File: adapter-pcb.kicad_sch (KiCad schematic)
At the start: 7 parts, among them J3 SS5-80-3.50-X-D-K-XX, M1 MountingHole_Pad_MP, M2 MountingHole_Pad_MP, M3 MountingHole_Pad_MP, M4 MountingHole_Pad_MP

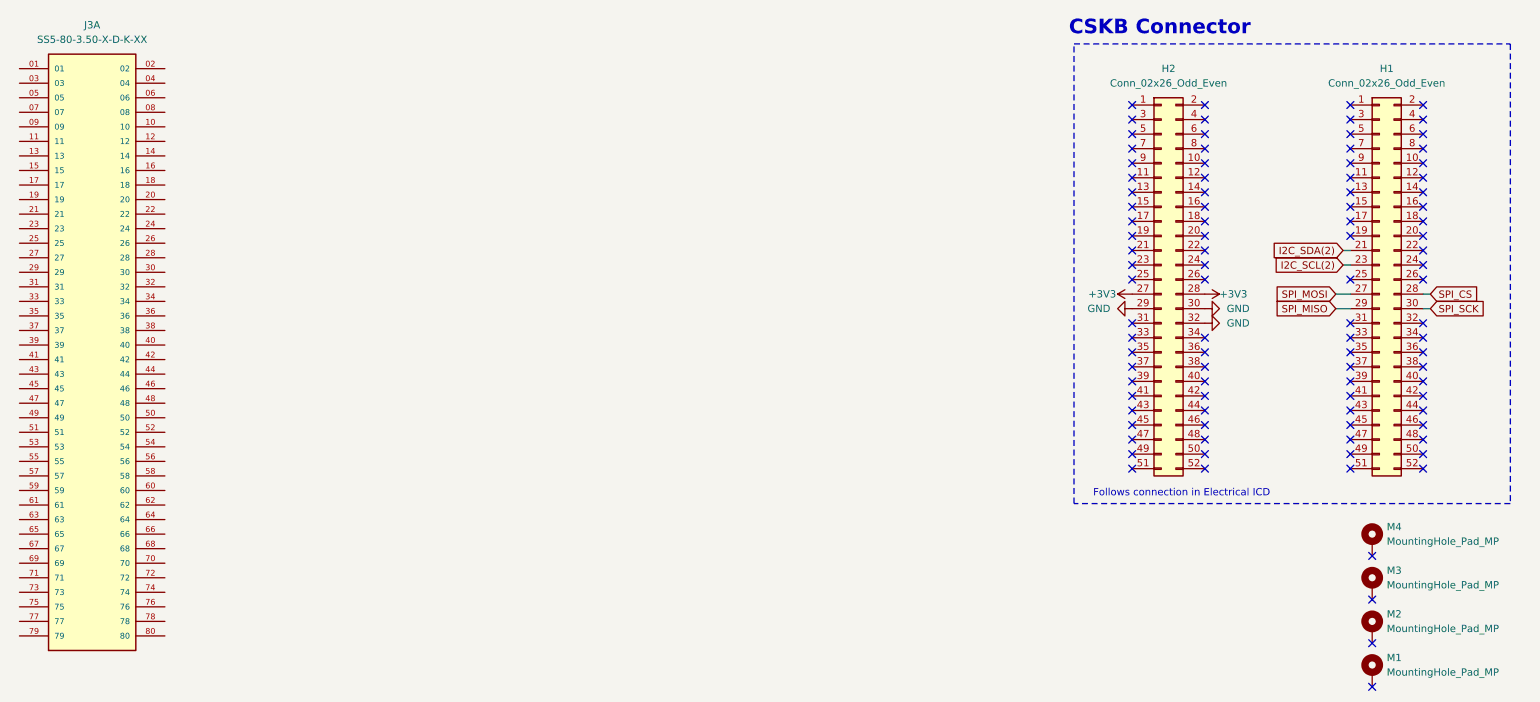
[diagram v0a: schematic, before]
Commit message: Routed PCB (with I2C buffer)
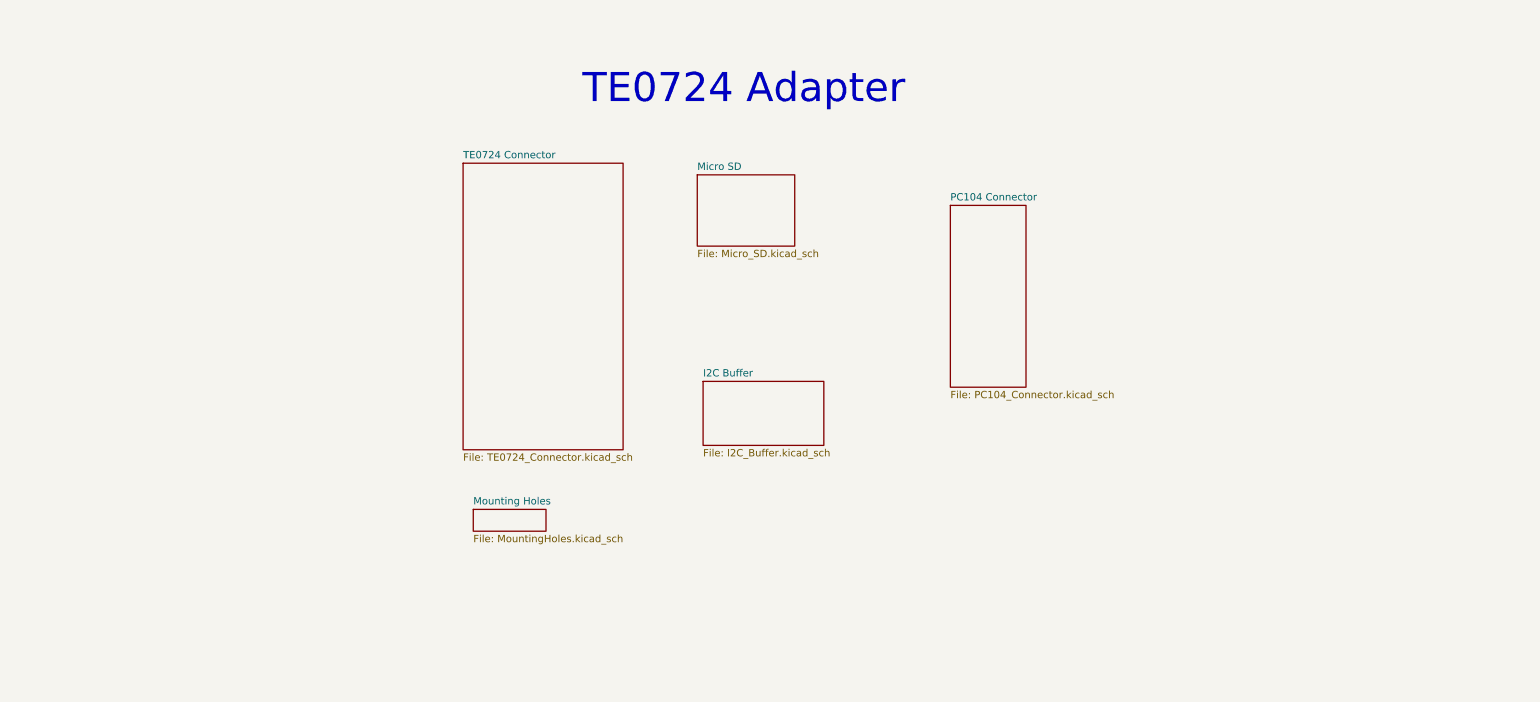
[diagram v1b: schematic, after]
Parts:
- removed H1, H2: Conn_02x26_Odd_Even, adapter:RHDR52W64P254_2X26_6654X495X1135P, symbol Connector_Generic:Conn_02x26_Odd_Even
- removed J3: SS5-80-3.50-X-D-K-XX, adapter:SAMTEC_SS5-80-3.50-X-D-K-XX, symbol adapter:SS5-80-3.50-X-D-K-XX
- removed M1, M2, M3, M4: MountingHole_Pad_MP, adapter:MountingHole_3.18mm_6.35mm_Pad, symbol Mechanical:MountingHole_Pad_MP
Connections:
- no-connect marks 97 -> 0
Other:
- added sheet I2C Buffer (I2C_Buffer.kicad_sch)
- added sheet Micro SD (Micro_SD.kicad_sch)
- added sheet Mounting Holes (MountingHoles.kicad_sch)
- added sheet PC104 Connector (PC104_Connector.kicad_sch)
- added sheet TE0724 Connector (TE0724_Connector.kicad_sch)
- note added: "TE0724 Adapter"
- note removed: "CSKB Connector"
- note removed: "Follows connection in Electrical ICD"
- title: (none) -> Overview

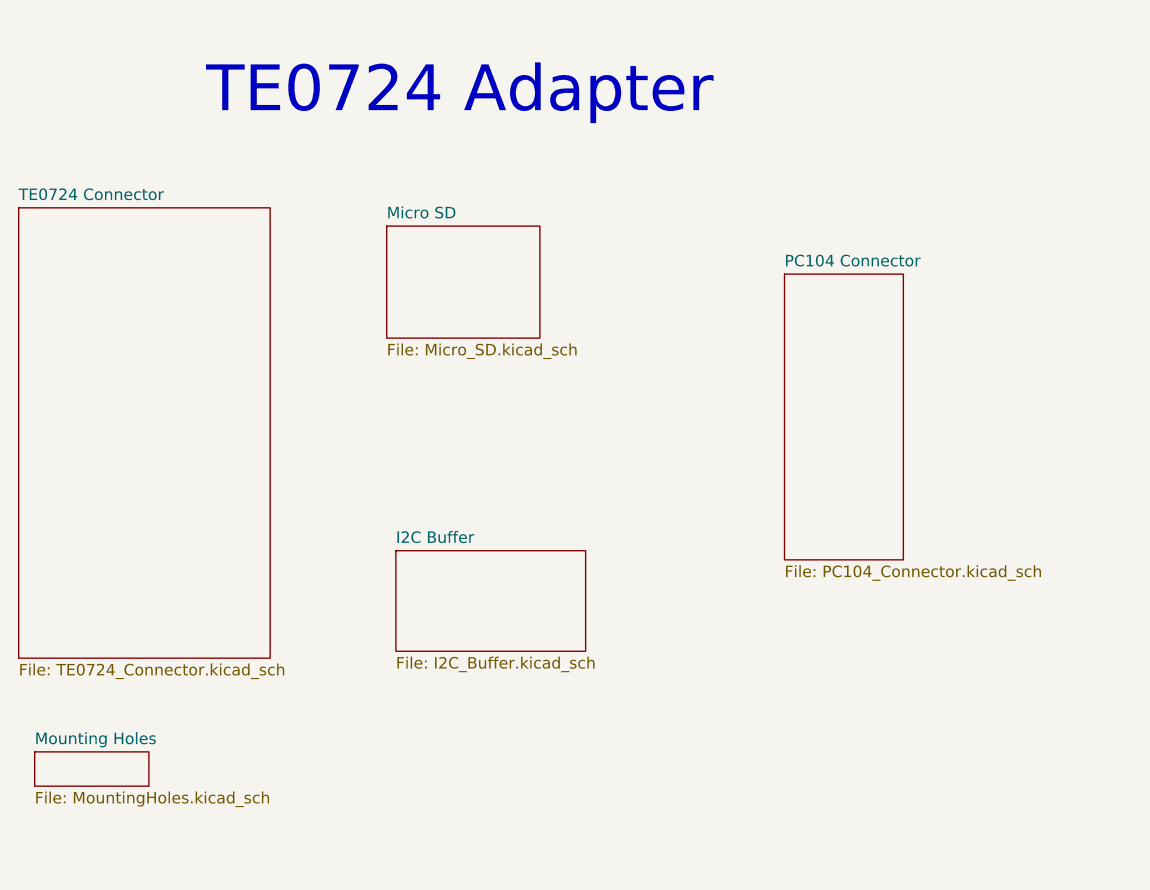
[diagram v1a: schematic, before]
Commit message: Fixed GND issues with connector and mounting holes
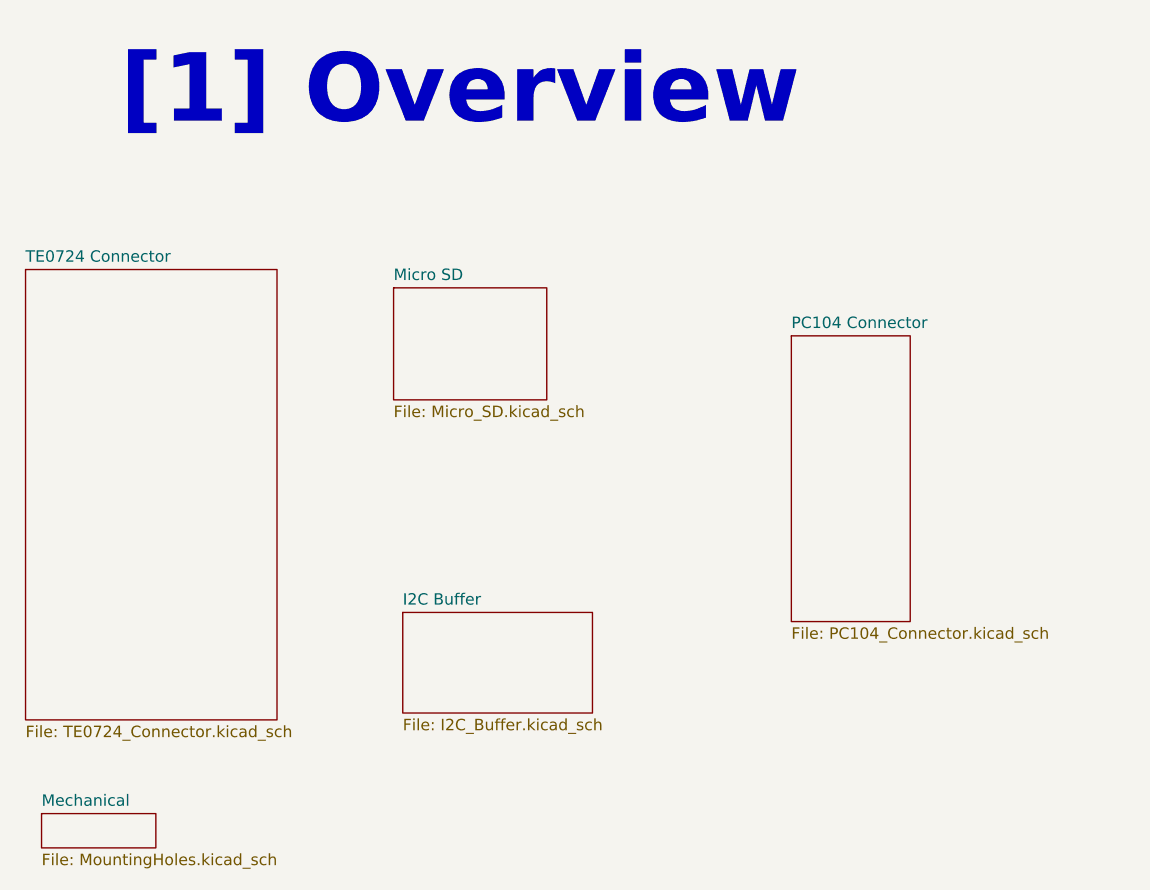
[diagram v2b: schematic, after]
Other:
- sheet Mounting Holes renamed Mechanical
- note added: "[1] Overview"
- note removed: "TE0724 Adapter"
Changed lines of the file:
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@@
 		(title "Overview")
 	)
-	(text "TE0724 Adapter"
+	(text "[1] Overview"
 		(exclude_from_sim no)
 		(at 146.812 27.686 0)
 		(effects
 			(font
-				(size 5.08 5.08)
-				(thickness 0.635)
-			)
-		)
-	)
-	(sheet
-		(at 138.684 42.672)
+				(size 7.62 7.62)
+				(thickness 1.524)
+				(bold yes)
+			)
+		)
+	)
+	(sheet
+		(at 139.446 49.53)
 		(size 17.018 12.446)
 		(exclude_from_sim no)
@@
 		)
 		(property "Sheetname" "Micro SD"
-			(at 138.684 41.9604 0)
+			(at 139.446 48.8184 0)
 			(effects
 				(font
@@
 		)
 		(property "Sheetfile" "Micro_SD.kicad_sch"
-			(at 138.684 55.7026 0)
+			(at 139.446 62.5606 0)
 			(effects
 				(font
@@
 	)
 	(sheet
-		(at 97.79 40.64)
+		(at 98.552 47.498)
 		(size 27.94 50.038)
 		(exclude_from_sim no)
@@
 		)
 		(property "Sheetname" "TE0724 Connector"
-			(at 97.79 39.9284 0)
+			(at 98.552 46.7864 0)
 			(effects
 				(font
@@
 		)
 		(property "Sheetfile" "TE0724_Connector.kicad_sch"
-			(at 97.79 91.2626 0)
+			(at 98.552 98.1206 0)
 			(effects
 				(font
@@
 	)
 	(sheet
-		(at 182.88 48.006)
+		(at 183.642 54.864)
 		(size 13.208 31.75)
 		(exclude_from_sim no)
@@
 		)
 		(property "Sheetname" "PC104 Connector"
-			(at 182.88 47.2944 0)
+			(at 183.642 54.1524 0)
 			(effects
 				(font
@@
 		)
 		(property "Sheetfile" "PC104_Connector.kicad_sch"
-			(at 182.88 80.3406 0)
+			(at 183.642 87.1986 0)
 			(effects
 				(font
@@
 	)
 	(sheet
-		(at 139.7 78.74)
+		(at 140.462 85.598)
 		(size 21.082 11.176)
 		(exclude_from_sim no)
@@
 		)
 		(property "Sheetname" "I2C Buffer"
-			(at 139.7 78.0284 0)
+			(at 140.462 84.8864 0)
 			(effects
 				(font
@@
 		)
 		(property "Sheetfile" "I2C_Buffer.kicad_sch"
-			(at 139.7 90.5006 0)
+			(at 140.462 97.3586 0)
 			(effects
 				(font
@@
 	)
 	(sheet
-		(at 99.568 101.092)
+		(at 100.33 107.95)
 		(size 12.7 3.81)
 		(exclude_from_sim no)
@@
 			(color 0 0 0 0.0000)
 		)
-		(property "Sheetname" "Mounting Holes"
-			(at 99.568 100.3804 0)
+		(property "Sheetname" "Mechanical"
+			(at 100.33 107.2384 0)
 			(effects
 				(font
@@
 		)
 		(property "Sheetfile" "MountingHoles.kicad_sch"
-			(at 99.568 105.4866 0)
-			(effects
-				(font
+			(at 100.33 112.3446 0)
+			(effects
+				(font
